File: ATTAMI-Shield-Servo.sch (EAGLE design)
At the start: 12 parts

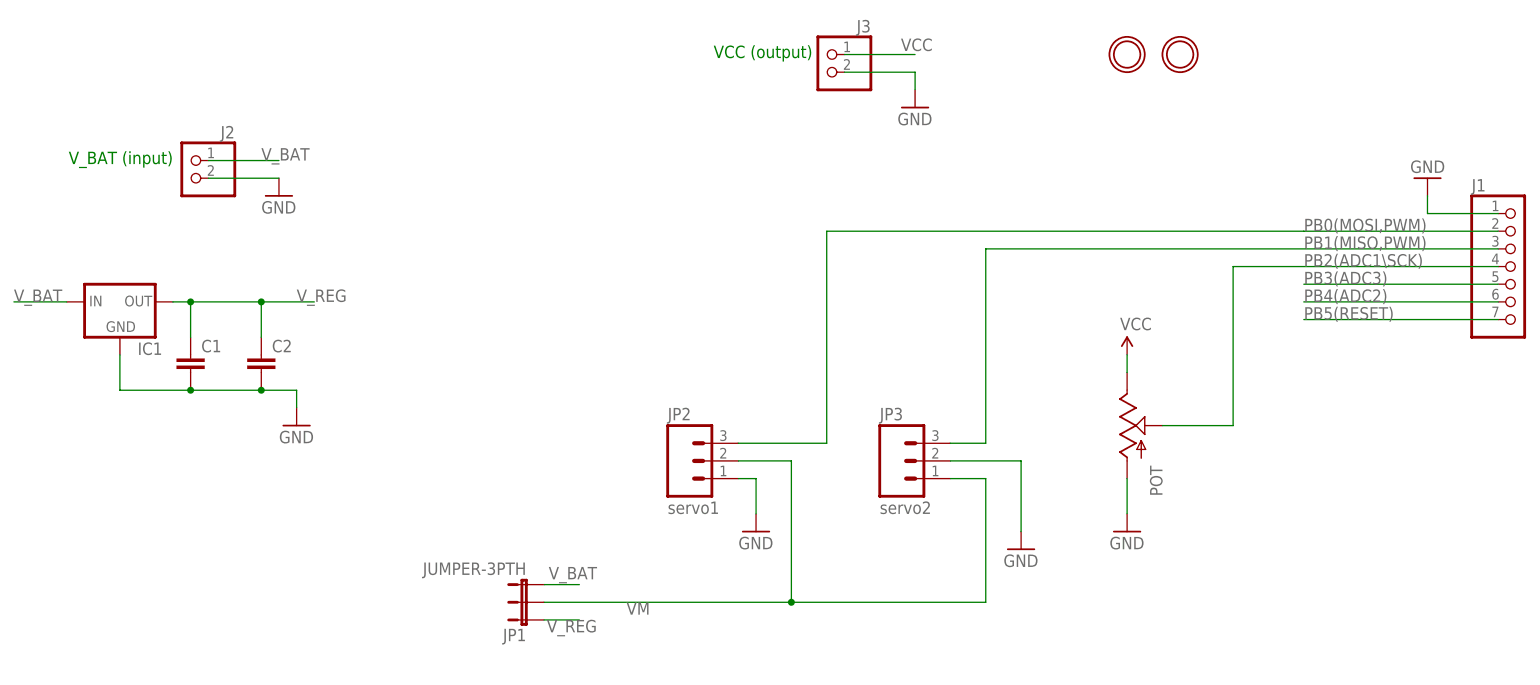
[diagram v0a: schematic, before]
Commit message: flipped servo power pins
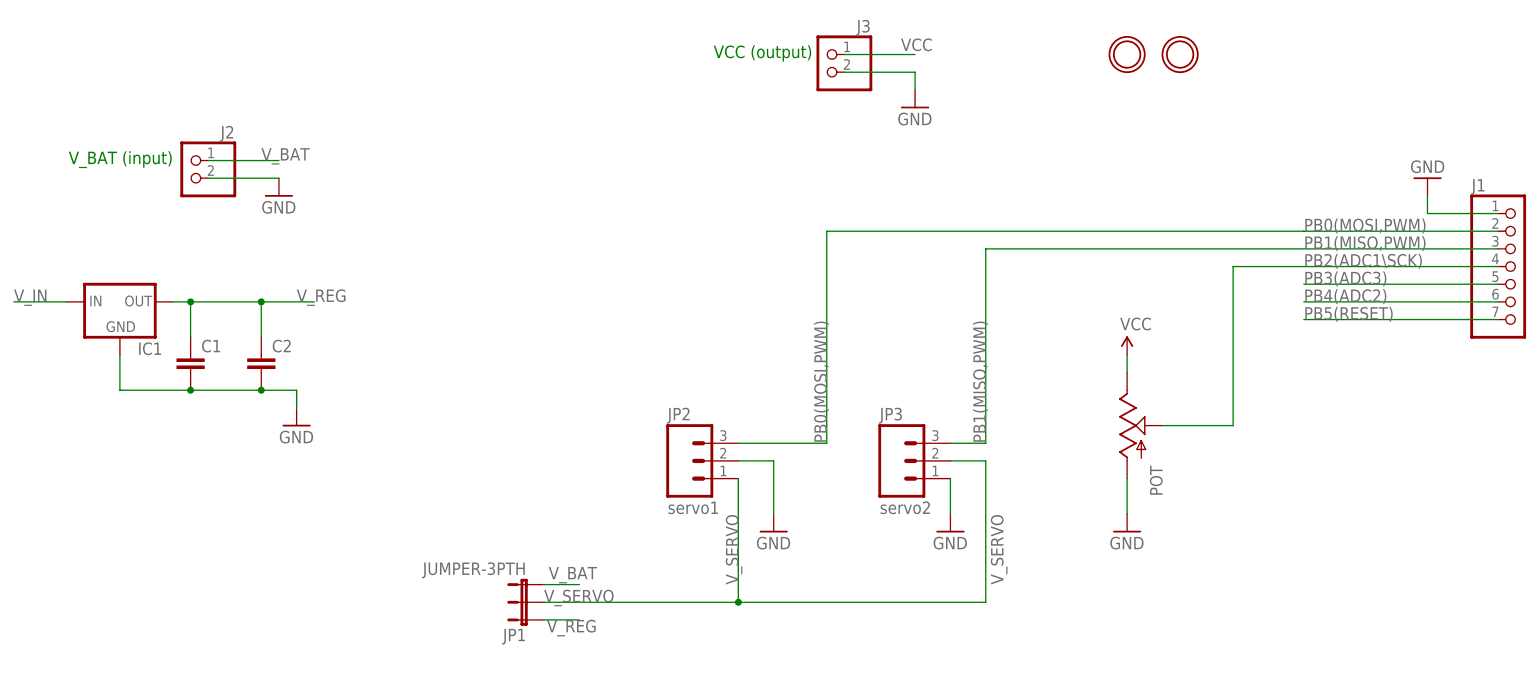
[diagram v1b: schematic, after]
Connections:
- removed net VM: JP1.2, JP2.2, JP3.1
- new net V_IN: IC1.IN
- new net V_SERVO: JP1.2, JP3.2
- net GND: now also JP2.2; no longer JP2.1, JP3.2
- net V_BAT: no longer IC1.IN
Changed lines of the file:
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@@
 <instance part="J1" gate="A" x="226.06" y="129.54"/>
 <instance part="GND2" gate="1" x="213.36" y="142.24" rot="R180"/>
-<instance part="GND3" gate="1" x="116.84" y="91.44"/>
-<instance part="GND4" gate="1" x="154.94" y="88.9"/>
+<instance part="GND3" gate="1" x="119.38" y="91.44"/>
+<instance part="GND4" gate="1" x="144.78" y="91.44"/>
 <instance part="C2" gate="G$1" x="45.72" y="114.3"/>
 <instance part="GND5" gate="1" x="170.18" y="91.44"/>
@@
 </segment>
 <segment>
-<pinref part="JP2" gate="G$1" pin="1"/>
 <pinref part="GND3" gate="1" pin="GND"/>
-<wire x1="114.3" y1="99.06" x2="116.84" y2="99.06" width="0.1524" layer="91"/>
-<wire x1="116.84" y1="99.06" x2="116.84" y2="93.98" width="0.1524" layer="91"/>
+<wire x1="119.38" y1="101.6" x2="119.38" y2="93.98" width="0.1524" layer="91"/>
+<pinref part="JP2" gate="G$1" pin="2"/>
+<wire x1="114.3" y1="101.6" x2="119.38" y2="101.6" width="0.1524" layer="91"/>
 </segment>
 <segment>
 <pinref part="GND4" gate="1" pin="GND"/>
-<pinref part="JP3" gate="G$1" pin="2"/>
-<wire x1="154.94" y1="101.6" x2="154.94" y2="91.44" width="0.1524" layer="91"/>
-<wire x1="144.78" y1="101.6" x2="154.94" y2="101.6" width="0.1524" layer="91"/>
+<wire x1="144.78" y1="99.06" x2="144.78" y2="93.98" width="0.1524" layer="91"/>
 </segment>
 <segment>
@@
 </segment>
 <segment>
-<pinref part="IC1" gate="G$1" pin="IN"/>
-<wire x1="17.78" y1="124.46" x2="10.16" y2="124.46" width="0.1524" layer="91"/>
-<label x="10.16" y="124.46" size="1.778" layer="95"/>
-</segment>
-<segment>
 <pinref part="JP1" gate="G$1" pin="3"/>
 <wire x1="86.36" y1="83.82" x2="91.44" y2="83.82" width="0.1524" layer="91"/>
@@
 <wire x1="127" y1="134.62" x2="127" y2="104.14" width="0.1524" layer="91"/>
 <wire x1="127" y1="104.14" x2="114.3" y2="104.14" width="0.1524" layer="91"/>
+<label x="127" y="104.14" size="1.778" layer="95" rot="R90"/>
 </segment>
 <segment>
@@
 <label x="195.58" y="132.08" size="1.778" layer="95"/>
 <wire x1="149.86" y1="132.08" x2="223.52" y2="132.08" width="0.1524" layer="91"/>
+<label x="149.86" y="104.14" size="1.778" layer="95" rot="R90"/>
 </segment>
 </net>
@@
 </segment>
 </net>
-<net name="VM" class="0">
+<net name="V_SERVO" class="0">
 <segment>
 <pinref part="JP1" gate="G$1" pin="2"/>
-<label x="101.6" y="81.28" size="1.778" layer="95" rot="R180"/>
-<wire x1="86.36" y1="81.28" x2="121.92" y2="81.28" width="0.1524" layer="91"/>
-<wire x1="121.92" y1="101.6" x2="121.92" y2="81.28" width="0.1524" layer="91"/>
-<pinref part="JP2" gate="G$1" pin="2"/>
-<wire x1="114.3" y1="101.6" x2="121.92" y2="101.6" width="0.1524" layer="91"/>
-<wire x1="121.92" y1="81.28" x2="149.86" y2="81.28" width="0.1524" layer="91"/>
-<wire x1="149.86" y1="81.28" x2="149.86" y2="99.06" width="0.1524" layer="91"/>
-<junction x="121.92" y="81.28"/>
-<pinref part="JP3" gate="G$1" pin="1"/>
-<wire x1="144.78" y1="99.06" x2="149.86" y2="99.06" width="0.1524" layer="91"/>
+<label x="86.36" y="81.28" size="1.778" layer="95"/>
+<wire x1="86.36" y1="81.28" x2="114.3" y2="81.28" width="0.1524" layer="91"/>
+<wire x1="114.3" y1="99.06" x2="114.3" y2="81.28" width="0.1524" layer="91"/>
+<wire x1="114.3" y1="81.28" x2="149.86" y2="81.28" width="0.1524" layer="91"/>
+<wire x1="149.86" y1="81.28" x2="149.86" y2="101.6" width="0.1524" layer="91"/>
+<junction x="114.3" y="81.28"/>
+<pinref part="JP3" gate="G$1" pin="2"/>
+<wire x1="149.86" y1="101.6" x2="144.78" y2="101.6" width="0.1524" layer="91"/>
+<label x="152.4" y="83.82" size="1.778" layer="95" rot="R90"/>
+<label x="114.3" y="83.82" size="1.778" layer="95" rot="R90"/>
 </segment>
 </net>
@@
 </segment>
 </net>
+<net name="V_IN" class="0">
+<segment>
+<pinref part="IC1" gate="G$1" pin="IN"/>
+<wire x1="17.78" y1="124.46" x2="10.16" y2="124.46" width="0.1524" layer="91"/>
+<label x="10.16" y="124.46" size="1.778" layer="95"/>
+</segment>
+</net>

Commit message: servo shield
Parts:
- added J4: (no value), microbuilder:HEADER-1X2ROUND
- JP1: value JUMPER-3PTH -> JUMPER-power
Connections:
- removed net V_REG: C1.1, C2.1, IC1.OUT, JP1.1
- removed net V_SERVO: JP1.2, JP3.2
- new net N$3: IC1.OUT, JP1.1
- net GND: now also J4.2, JP2.1, JP3.1; no longer JP2.2
- net VCC: no longer J3.1
- net V_BAT: now also C1.1, C2.1, JP1.2, JP2.2, JP3.2; no longer JP1.3
- net V_IN: now also J3.1, J4.1, JP1.3
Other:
- note added: "5-7V input"
- note added: "7-12V input"
- note added: "V_BAT"
- note added: "keep V_BAT header unexposed to shield users. as in, only facing down to main board. power will come from either 1. V_IN -> V_BAT 2. V_IN -> V_REG -> V_BAT"
- note added: "more at github.com/telavivmakers/at-tami Notes:"
- note removed: "VCC (output)"
- note removed: "V_BAT (input)"
- note removed: "more at github.com/telavivmakers/at-tami Notes: 1. D1 and D2 are Blue LEDs they might not light when using Vi_BAT <4V~ 2. When VCC is less than 5V change the system clock of the ATTINY85 to 8MHz or less - refer to the datasheet P163 Section 21-3 Speed"
- moved on the sheet: C1, C2, IC1, J2, J3, JP1, JP2, JP3
